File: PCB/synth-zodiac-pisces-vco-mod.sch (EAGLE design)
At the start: 59 parts, among them Q1 PMP4201, U3 LM393, U4 TL074A, U5 CD4066

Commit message: Snapshot of designs so far.
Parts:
- removed BIAS: NP, rlc:TRIMPOTTC33X
- removed C1: 4700pF, rlc:CAPACITOR0603
- removed C10: 220pF, rlc:CAPACITOR0603
- removed C2: 22uF, rlc:CAPACITOR0603
- removed C3, C4, C6, C7: 0.1uF, rlc:CAPACITOR0603
- removed C5: 3900pF, rlc:CAPACITOR0603
- removed C8: 1.0uF, rlc:CAPACITOR0603
- removed C9: 100pF, rlc:CAPACITOR0603
- removed CONST1: Aquarius, circuit-monkey-zodiac:CONSTELLATION-AQUARIUS
- removed CP_EXP_VCO, CP_GND, CP_VCO_LIN_FM, CP_VCO_OUT: PADSMD-070X070, con-testpoints:PADSMD-070X070
- removed D1, D2: 1N4148, diodes:DIODE-1N4148
- removed EXP_VCO_TRIM: 100K - NP, rlc:TRIMPOTTC33X
- removed FREQ: 10K, rlc:TRIMPOT9MM_PCB_SHAFT
- removed J1: (no value), con-jst:04P-VT-SMT
- removed KB_CV, VCO_MOD_CV, VCO_OUT: 2-pin, VT, SMT, con-jst:02PVT-SMT
- removed KB_TRIM: 100K, rlc:TRIMPOTTC33X
- removed PULSE, SAW, TP4: TPSMD-040-RND, con-testpoints:TPSMD-040-RND
- removed Q1: PMP4201, transistor-bjt:NPN-DUALPMP4201
- removed R10, R11, R13, R14, R24: 0, rlc:RESISTOR0603
- removed R12: NS, rlc:RESISTOR0603
- removed R15, R16: 100K, rlc:RESISTOR0603
- removed R17: 10.0K, rlc:RESISTOR0603
- removed R18: 4.75M, rlc:RESISTOR0603
- removed R19, R20, R21, R22: 4.99K, rlc:RESISTOR0603
- removed R2, R3: 221K, rlc:RESISTOR0603
- removed R23, R9: 10K, rlc:RESISTOR0603
- removed R4: 412K, rlc:RESISTOR0603
- removed R5: 68.1K - NP, rlc:RESISTOR0603
- removed R6: 2.2K, rlc:RESISTOR0603
- removed R7: 499K, rlc:RESISTOR0603
- removed R8: 1.82M, rlc:RESISTOR0603
- removed TYPE: SPDT, switch-thd:SLIDE-SPDTSS-12-F45-TH-PCB
- removed U3: LM393, op-amp:DUAL-LM393ED
- removed U4: TL074A, op-amp:QUADTL074A-SOIC
- removed U5: CD4066, logic:CD4066SO14
- added AMP: TL071, op-amp:SINGLE-TL071
- added AMT, PWM: 10K, rlc:TRIMPOT9MM_PCB_SHAFT
- added C41, C42: 0.1uF, rlc:CAPACITOR0603
- added CONST: Pisces, circuit-monkey-zodiac:CONSTELLATION-PISCES
- added CP_VCO_MOD: PADSMD-070X070, con-testpoints:PADSMD-070X070
- added EG, LFO, VCO_MOD: 2-pin, VT, SMT, con-jst:02PVT-SMT
- added MOD_SRC: SPDT, switch-thd:SLIDE-SPDTSS-12-F45-TH-PCB
- added PULSE_WIDTH: DPDT, switch-thd:SLIDE-DPDT-MNTPNL-SMD
- added PWR: (no value), con-jst:04P-VT-SMT
- added R70: 4.99K, rlc:RESISTOR0603
- added R71: 47.5R, rlc:RESISTOR0603
- GLYPH: value Aquarius -> Capricorn; device circuit-monkey-zodiac:GLYPH-AQUARIUS -> circuit-monkey-zodiac:GLYPH-CAPRICORN
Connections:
- removed net BIAS: BIAS.2, R19.2, R20.1, R21.1
- removed net EXP_VCO_CV_IN: CP_EXP_VCO.PAD, EXP_VCO_TRIM.1
- removed net EXP_VCO_LIN_FM: CP_VCO_LIN_FM.PAD, R7.1
- removed net FREQ: FREQ.2, R2.1
- removed net FREQ_CV_MIX: C1.1, R2.2, R3.2, R4.2, R5.2, R6.1, U4-A.-
- removed net KB_CV: KB_CV.1, KB_TRIM.1
- removed net N$12: Q1-A.EMITTER, R7.2, R8.2, U4-B.+
- removed net N$13: Q1-B.EMITTER, U4-B.-, U4-B.OUT
- removed net N$14: C1.2, Q1-A.BASE, R6.2, U4-A.OUT
- removed net N$15: R12.2, R9.2, U5-A.EN, U5-B.EN, U5-C.IN
- removed net N$16: C9.1, R17.1, R18.1, U4-D.+
- removed net N$17: R14.2, U3-B.-
- removed net N$18: C9.2, D1.A, R18.2, U4-D.OUT
- removed net N$20: C5.2, Q1-B.COLLECTOR, U4-C.+, U5-A.OUT
- removed net N$21: BIAS.3, C8.2, R17.2, R19.1
- removed net N$22: C10.1, R21.2, U5-B.IN
- removed net N$23: R12.1, U5-D.OUT
- removed net N$24: D1.K, D2.K, R23.1, U5-C.EN
- removed net N$25: R10.2, U5-D.IN
- removed net N$26: R11.2, U5-D.EN
- removed net N$27: R13.2, U3-B.+
- removed net N$28: R15.2, R16.1, U3-A.-
- removed net N$29: TP4.P$1, U3-B.OUT
- removed net N$8: KB_TRIM.2, KB_TRIM.3, R4.1
- removed net N$9: EXP_VCO_TRIM.2, EXP_VCO_TRIM.3, R5.1
- removed net PULSE: PULSE.P$1, R22.2, TYPE-SW.B, U3-A.OUT
- removed net SAW: R24.2, TYPE-SW.A
- removed net VCO_CORE: R24.1, SAW.P$1, U3-A.+, U4-C.-, U4-C.OUT, U4-D.-
- removed net VCO_OUT: CP_VCO_OUT.PAD, TYPE-SW.C, VCO_OUT.1
- new net EG: EG.1, MOD_SRC-SW.B
- new net LFO_CV: LFO.1, MOD_SRC-SW.A
- new net MOD_CORE: AMPG.-, AMPG.OUT, PULSE_WIDTH-SW.1A, PULSE_WIDTH-SW.2B
- new net N$100: PULSE_WIDTH-SW.1B, PWM.2
- new net N$86: AMPG.+, AMT.2
- new net N$97: PWM.1, R70.1
- new net N$98: PWM.3, R71.2
- new net VCO_SRC: AMT.3, MOD_SRC-SW.C
- net +5V: now also PWR.3, R71.1; no longer C2.2, C5.1, J1.3, R16.2, R22.1, U5-A.IN
- net +9V: now also AMPPWR.V+, C41.1, PWR.1; no longer C10.2, C3.2, C6.2, C7.2, FREQ.3, J1.1, U3-PWR.V+, U4-PWR.V+, U5-B.OUT, U5-C.OUT, U5-PWR.VCC
- net -9V: now also AMPPWR.V-, C42.2, PWR.2; no longer C4.1, FREQ.1, J1.2, R8.1, U4-PWR.V-
- net GND: now also AMT.1, C41.2, C42.1, EG.2, LFO.2, MOD_SRC-MTG.MT1, MOD_SRC-MTG.MT2, PULSE_WIDTH-MNT.MT1, PULSE_WIDTH-MNT.MT2, PULSE_WIDTH-SW.2A, PWR.4, R70.2, VCO_MOD.2; no longer BIAS.1, C2.1, C3.1, C4.2, C6.1, C7.1, C8.1, CP_GND.PAD, D2.A, J1.4, KB_CV.2, Q1-A.COLLECTOR, Q1-B.BASE, R10.1, R11.1, R13.1, R14.1, R20.2, R23.2, R9.1, TYPE-MTG.MT1, TYPE-MTG.MT2, U3-PWR.V-, U4-A.+, U5-PWR.GND, VCO_MOD_CV.2, VCO_OUT.2
- net PWM_CV: now also PULSE_WIDTH-SW.1C; no longer R15.1
- net VCO_MOD_CV: now also CP_VCO_MOD.PAD, PULSE_WIDTH-SW.2C, VCO_MOD.1; no longer R3.1, VCO_MOD_CV.1
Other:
- note added: "===> VCO"
- note added: "===> VCO / CV_PNL"
- note added: "EG ===>"
- note added: "LFO ===>"
- note added: "Pulse Width"
- note added: "VCO MODULATOR"
- note added: "VCO Modulation Source"
- note removed: "=> VCF / CV_PNL"
- note removed: "Aquarius"
- note removed: "CP =>"
- note removed: "KB =>"
- note removed: "PULSE"
- note removed: "SAW"
- note removed: "VCO"
- note removed: "VCO FREQ"
- note removed: "VCO WAVE"
- note removed: "VCO_MOD =>"
- note removed: "Zodiac Synth"
- moved on the sheet: GLYPH, PCB, PWM_CV

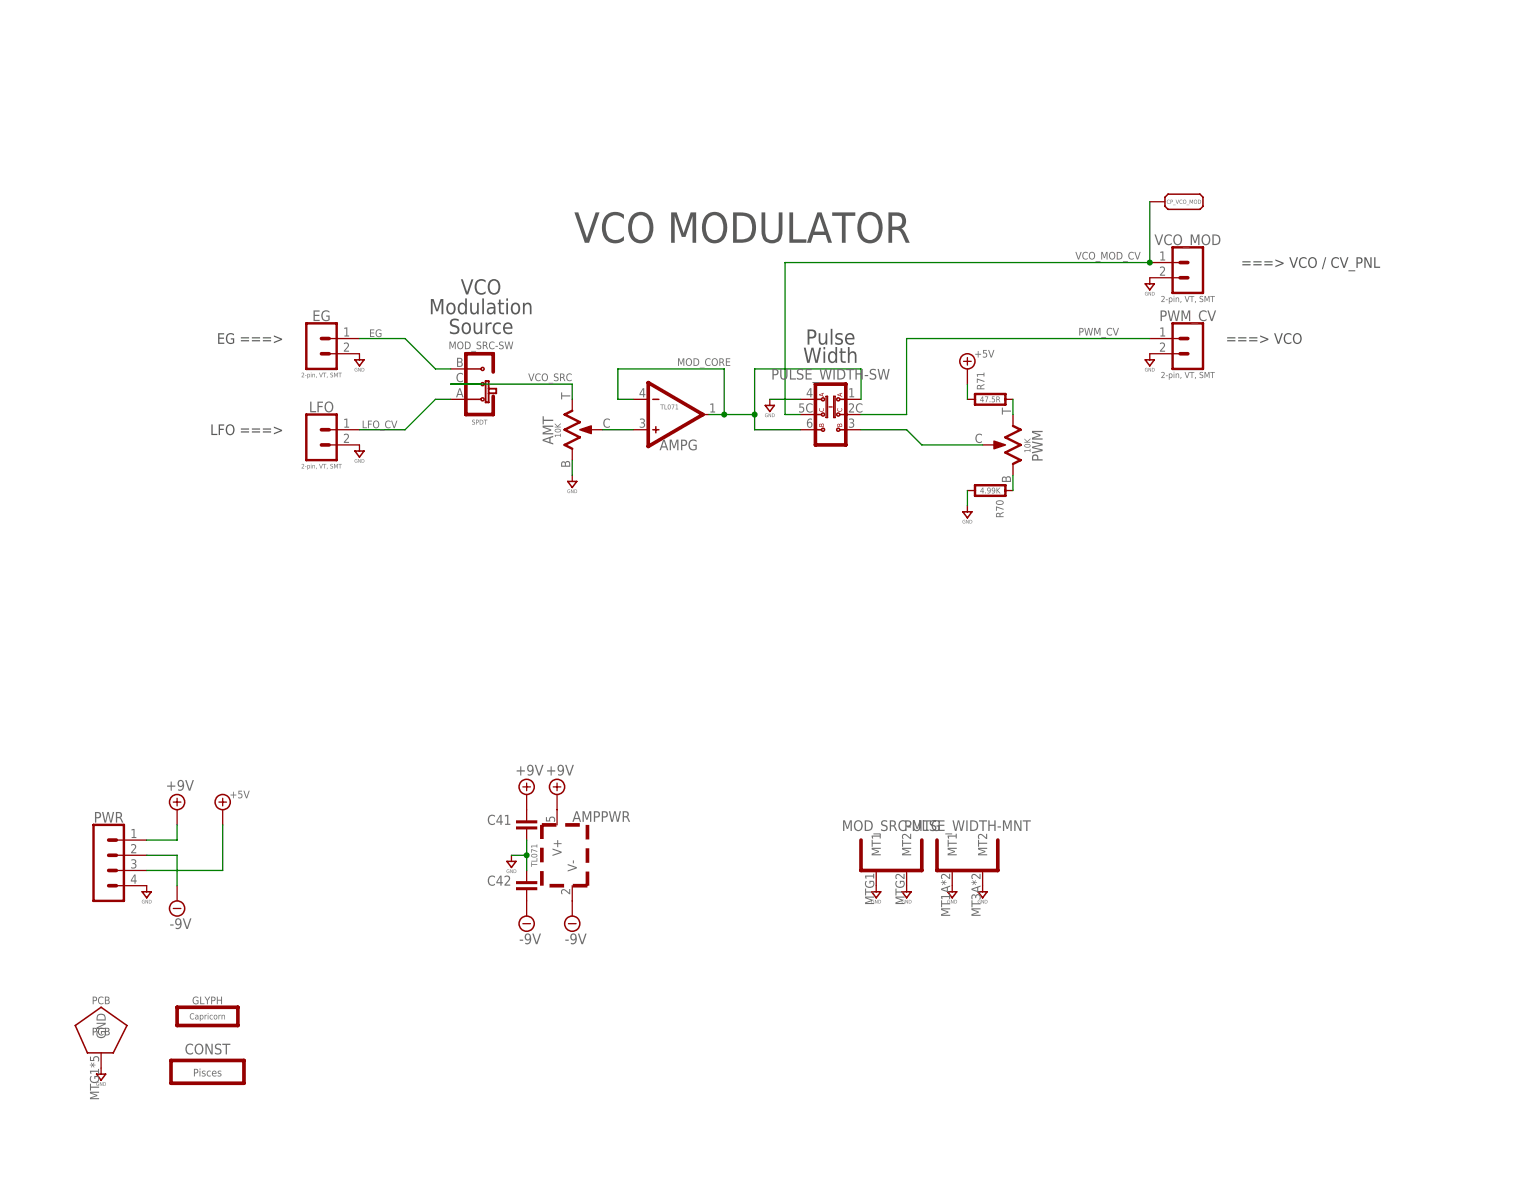
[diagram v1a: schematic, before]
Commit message: Almost ready for FAB.
Sagittarius was mis-spelled, renamed it.  Taurus is still WIP.
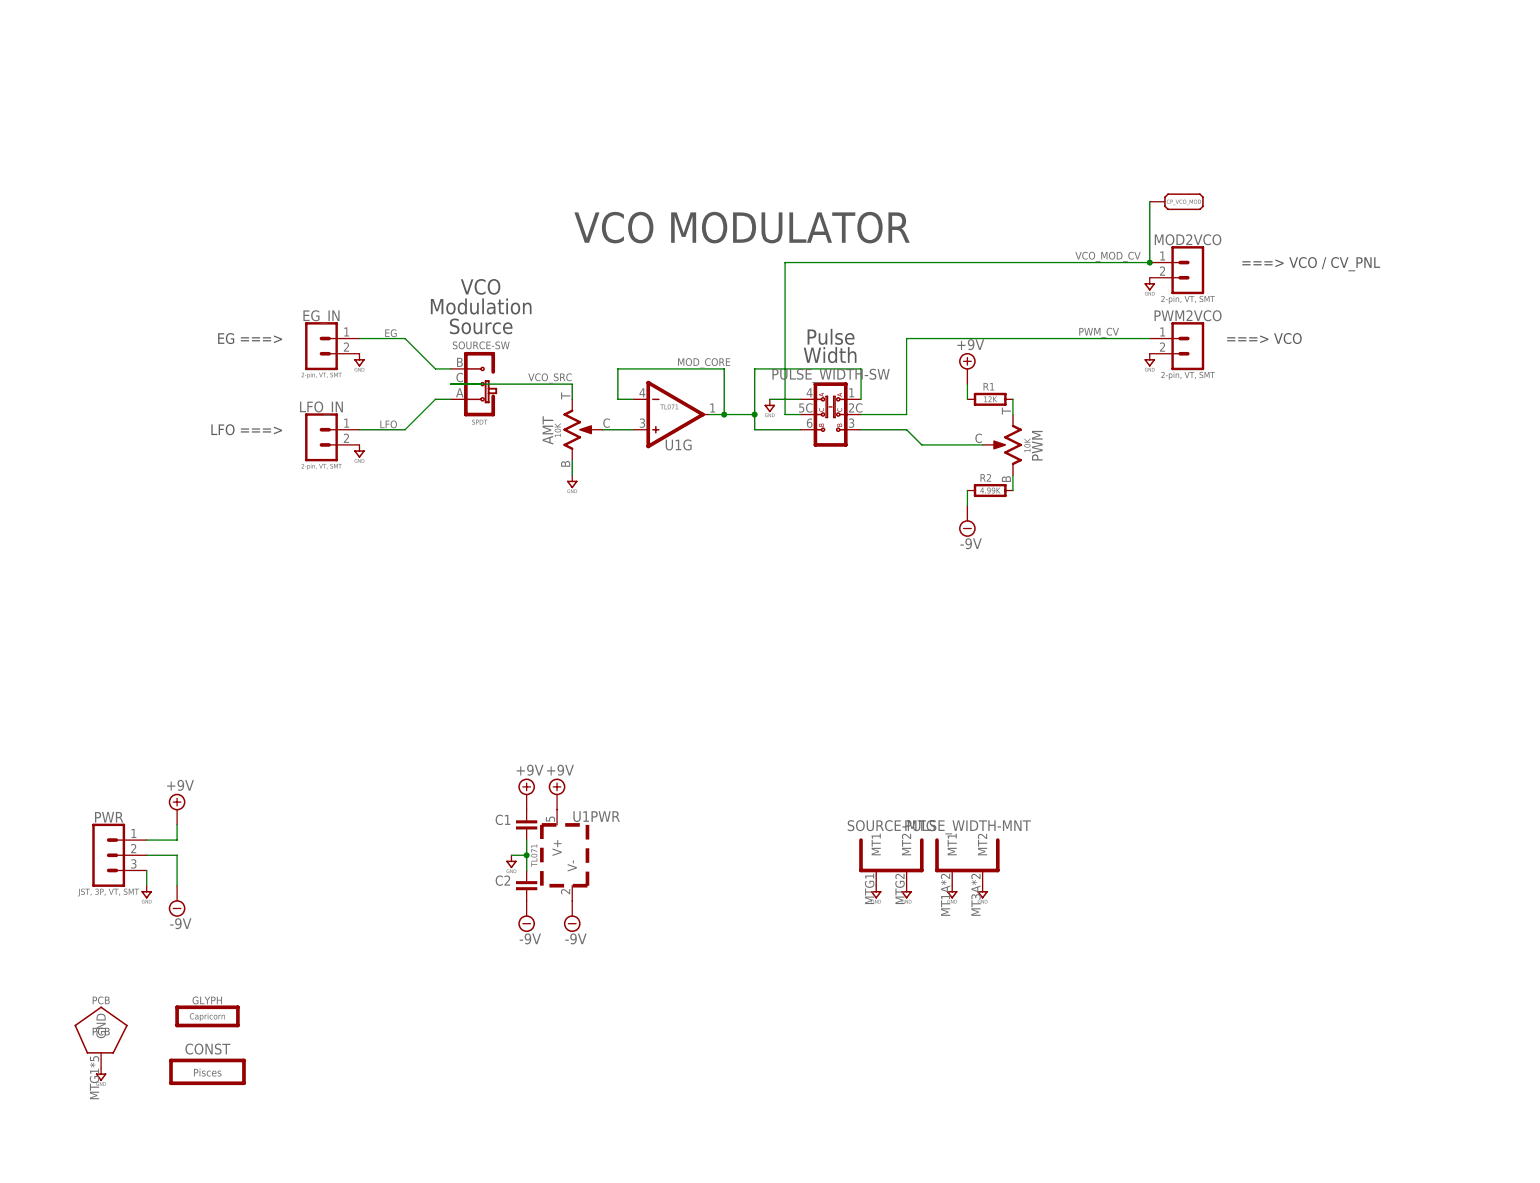
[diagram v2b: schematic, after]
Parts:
- PWR: value (none) -> JST, 3P, VT, SMT; device con-jst:04P-VT-SMT -> con-jst:03P-VT-SMT
- R1: value 47.5R -> 12K
- renumbered AMP to U1, C41 to C1, C42 to C2, EG to EG_IN, LFO to LFO_IN, MOD_SRC to SOURCE, PWM_CV to PWM2VCO, R70 to R2, R71 to R1, VCO_MOD to MOD2VCO
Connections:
- net LFO_CV renamed LFO
- removed net +5V: PWR.3, R1.1
- net +9V: now also R1.1
- net -9V: now also R2.2
- net GND: now also PWR.3; no longer PWR.4, R2.2

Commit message: Work in progress for rev A,  VCO rev.B
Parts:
- removed SOURCE: SPDT, switch-thd:SLIDE-SPDTSS-12-F45-TH-PCB
- added PWMADJ: JST, SH, 2P, con-jst:02P-SM-VT-SMT
- added SRC: (no value), switch-thd:SLIDE-SPDT-MNTSS-12-F45-TH-PCB
- EG_IN, LFO_IN, MOD2VCO, PWM2VCO: value 2-pin, VT, SMT -> JST, SH, 2P; device con-jst:02PVT-SMT -> con-jst:02P-SM-VT-SMT
- PWR: value JST, 3P, VT, SMT -> JST SM 3P; device con-jst:03P-VT-SMT -> con-jst:03P-SM-VT-SMT
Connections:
- removed net N$100: PULSE_WIDTH-SW.1B, PWM.2
- new net PWM_ADJ: PULSE_WIDTH-SW.1B, PWM.2, PWMADJ.1
- net EG: now also SRC-SW.B; no longer SOURCE-SW.B
- net GND: now also PWMADJ.2, SRC-MTG.MT1, SRC-MTG.MT2; no longer SOURCE-MTG.MT1, SOURCE-MTG.MT2
- net LFO: now also SRC-SW.A; no longer SOURCE-SW.A
- net VCO_SRC: now also SRC-SW.C; no longer SOURCE-SW.C
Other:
- note added: "Pisces"
- note added: "SATAN'S CYCLE WORKS"
- note added: "VCO MOD"
- note added: "Zodiac Synth"
- moved on the sheet: AMT, C1, C2, CONST, CP_VCO_MOD, EG_IN, GLYPH, LFO_IN, MOD2VCO, PCB, PULSE_WIDTH-MNT, PULSE_WIDTH-SW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

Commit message: Perhaps final Rev. A?
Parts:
- PULSE_WIDTH: value DPDT -> Switch, DPDT; device switch-thd:SLIDE-DPDT-MNTPNL-SMD -> switch-thd:SLIDE-DPDT-MNTPNL-SMD-TOGGLE-ONLY
- SRC: device switch-thd:SLIDE-SPDT-MNTSS-12-F45-TH-PCB -> switch-thd:SLIDE-SPDT-MNTSS-12-F45-TH-PCB-2
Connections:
- net EG: now also SRC-SW.A; no longer SRC-SW.B
- net LFO: now also SRC-SW.B; no longer SRC-SW.A
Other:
- moved on the sheet: SRC-MTG, SRC-SW
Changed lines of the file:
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@@
 <part name="R2" library="rlc" library_urn="urn:adsk.eagle:library:4192893" deviceset="RESISTOR" device="0603" package3d_urn="urn:adsk.eagle:package:4193040/5" value="4.99K"/>
 <part name="R1" library="rlc" library_urn="urn:adsk.eagle:library:4192893" deviceset="RESISTOR" device="0603" package3d_urn="urn:adsk.eagle:package:4193040/5" value="12K"/>
-<part name="C1" library="rlc" library_urn="urn:adsk.eagle:library:4192893" deviceset="CAPACITOR" device="0603" package3d_urn="urn:adsk.eagle:package:4193021/4" value="0.1uF"/>
-<part name="C2" library="rlc" library_urn="urn:adsk.eagle:library:4192893" deviceset="CAPACITOR" device="0603" package3d_urn="urn:adsk.eagle:package:4193021/4" value="0.1uF"/>
+<part name="C1" library="rlc" library_urn="urn:adsk.eagle:library:4192893" deviceset="CAPACITOR" device="0603" package3d_urn="urn:adsk.eagle:package:4193021/5" value="0.1uF"/>
+<part name="C2" library="rlc" library_urn="urn:adsk.eagle:library:4192893" deviceset="CAPACITOR" device="0603" package3d_urn="urn:adsk.eagle:package:4193021/5" value="0.1uF"/>
 <part name="SUPPLY95" library="supply" library_urn="urn:adsk.eagle:library:10485988" deviceset="GND" device=""/>
 <part name="SUPPLY101" library="supply" library_urn="urn:adsk.eagle:library:10485988" deviceset="-9V" device=""/>
@@
 <part name="SUPPLY106" library="supply" library_urn="urn:adsk.eagle:library:10485988" deviceset="+9V" device=""/>
 <part name="SUPPLY107" library="supply" library_urn="urn:adsk.eagle:library:10485988" deviceset="+9V" device=""/>
-<part name="PULSE_WIDTH" library="switch-thd" library_urn="urn:adsk.eagle:library:26242324" deviceset="SLIDE-DPDT-MNT" device="PNL-SMD" package3d_urn="urn:adsk.eagle:package:36475163/1" value="DPDT"/>
+<part name="PULSE_WIDTH" library="switch-thd" library_urn="urn:adsk.eagle:library:26242324" deviceset="SLIDE-DPDT-MNT" device="PNL-SMD-TOGGLE-ONLY" value="Switch, DPDT"/>
 <part name="SUPPLY167" library="supply" library_urn="urn:adsk.eagle:library:10485988" deviceset="GND" device=""/>
 <part name="SUPPLY168" library="supply" library_urn="urn:adsk.eagle:library:10485988" deviceset="GND" device=""/>
 <part name="SUPPLY205" library="supply" library_urn="urn:adsk.eagle:library:10485988" deviceset="GND" device=""/>
 <part name="SUPPLY206" library="supply" library_urn="urn:adsk.eagle:library:10485988" deviceset="GND" device=""/>
-<part name="AMT" library="rlc" library_urn="urn:adsk.eagle:library:4192893" deviceset="TRIMPOT" device="9MM_PCB_SHAFT" package3d_urn="urn:adsk.eagle:package:36472483/2" value="10K"/>
-<part name="PWM" library="rlc" library_urn="urn:adsk.eagle:library:4192893" deviceset="TRIMPOT" device="9MM_PCB_SHAFT" package3d_urn="urn:adsk.eagle:package:36472483/2" value="10K"/>
+<part name="AMT" library="rlc" library_urn="urn:adsk.eagle:library:4192893" deviceset="TRIMPOT" device="9MM_PCB_SHAFT" package3d_urn="urn:adsk.eagle:package:36472483/3" value="10K"/>
+<part name="PWM" library="rlc" library_urn="urn:adsk.eagle:library:4192893" deviceset="TRIMPOT" device="9MM_PCB_SHAFT" package3d_urn="urn:adsk.eagle:package:36472483/3" value="10K"/>
 <part name="PCB" library="circuit-monkey-zodiac" library_urn="urn:adsk.eagle:library:36060312" deviceset="PENTAGON" device="-40R" package3d_urn="urn:adsk.eagle:package:36376820/2" value="PCB FAB"/>
 <part name="SUPPLY1" library="supply" library_urn="urn:adsk.eagle:library:10485988" deviceset="GND" device=""/>
@@
 <part name="PWMADJ" library="con-jst" library_urn="urn:adsk.eagle:library:7191852" deviceset="02P" device="-SM-VT-SMT" package3d_urn="urn:adsk.eagle:package:41368283/6" value="JST, SH, 2P"/>
 <part name="SUPPLY9" library="supply" library_urn="urn:adsk.eagle:library:10485988" deviceset="GND" device=""/>
-<part name="SRC" library="switch-thd" library_urn="urn:adsk.eagle:library:26242324" deviceset="SLIDE-SPDT-MNT" device="SS-12-F45-TH-PCB" package3d_urn="urn:adsk.eagle:package:36475164/3"/>
+<part name="SRC" library="switch-thd" library_urn="urn:adsk.eagle:library:26242324" deviceset="SLIDE-SPDT-MNT" device="SS-12-F45-TH-PCB-2"/>
 </parts>
 <sheets>
@@
 <attribute name="VALUE" x="190.5" y="70.993" size="0.6096" layer="96" font="vector" align="center"/>
 </instance>
-<instance part="SRC" gate="-SW" x="76.2" y="106.68" smashed="yes" rot="MR90">
-<attribute name="NAME" x="80.264" y="106.68" size="1.778" layer="95" ratio="15" rot="MR90" align="center"/>
-<attribute name="VALUE" x="81.788" y="106.934" size="0.8128" layer="96" rot="MR90" align="center"/>
+<instance part="SRC" gate="-SW" x="76.2" y="106.68" smashed="yes" rot="R270">
+<attribute name="NAME" x="80.264" y="106.68" size="1.778" layer="95" ratio="15" rot="R270" align="center"/>
+<attribute name="VALUE" x="81.788" y="106.426" size="0.8128" layer="96" rot="R270" align="center"/>
 </instance>
 <instance part="SRC" gate="-MTG" x="27.94" y="12.7" smashed="yes">
@@
 <net name="LFO" class="0">
 <segment>
-<wire x1="71.12" y1="104.14" x2="68.58" y2="104.14" width="0.1524" layer="91"/>
 <wire x1="68.58" y1="104.14" x2="63.5" y2="99.06" width="0.1524" layer="91"/>
 <wire x1="63.5" y1="99.06" x2="55.88" y2="99.06" width="0.1524" layer="91"/>
 <label x="62.23" y="99.314" size="1.27" layer="95" rot="MR0"/>
 <pinref part="LFO_IN" gate="G$1" pin="1"/>
-<pinref part="SRC" gate="-SW" pin="A"/>
+<pinref part="SRC" gate="-SW" pin="B"/>
+<wire x1="68.58" y1="104.14" x2="71.12" y2="104.14" width="0.1524" layer="91"/>
 </segment>
 </net>
@@
 <net name="EG" class="0">
 <segment>
-<wire x1="71.12" y1="109.22" x2="68.58" y2="109.22" width="0.1524" layer="91"/>
 <wire x1="68.58" y1="109.22" x2="63.5" y2="114.3" width="0.1524" layer="91"/>
 <wire x1="63.5" y1="114.3" x2="55.88" y2="114.3" width="0.1524" layer="91"/>
 <label x="62.23" y="114.554" size="1.27" layer="95" rot="MR0"/>
 <pinref part="EG_IN" gate="G$1" pin="1"/>
-<pinref part="SRC" gate="-SW" pin="B"/>
-</segment>
-</net>
+<pinref part="SRC" gate="-SW" pin="A"/>
+<wire x1="68.58" y1="109.22" x2="71.12" y2="109.22" width="0.1524" layer="91"/>
+</segment>
+</net>

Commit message: Tune values and some schematic visual tweaks.
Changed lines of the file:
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@@
 <instance part="C1" gate="G$1" x="43.18" y="53.34" smashed="yes" rot="MR0">
 <attribute name="NAME" x="40.64" y="53.34" size="1.6764" layer="95" font="vector" ratio="15" rot="MR0"/>
+<attribute name="VALUE" x="40.64" y="52.324" size="0.6096" layer="96" font="vector" rot="MR0"/>
 </instance>
 <instance part="C2" gate="G$1" x="43.18" y="43.18" smashed="yes" rot="MR0">
 <attribute name="NAME" x="40.64" y="43.18" size="1.6764" layer="95" font="vector" ratio="15" rot="MR0"/>
+<attribute name="VALUE" x="40.64" y="42.164" size="0.6096" layer="96" font="vector" rot="MR0"/>
 </instance>
 <instance part="SUPPLY95" gate="GND" x="40.64" y="48.26" smashed="yes">
